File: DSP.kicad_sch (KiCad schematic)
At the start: 24 parts, among them J2 Conn_01x04, J3 MEM2067-02-180-00-A_REVB, J5 Conn_01x04, U4 STM32F401RBTx, Y1 16MHz

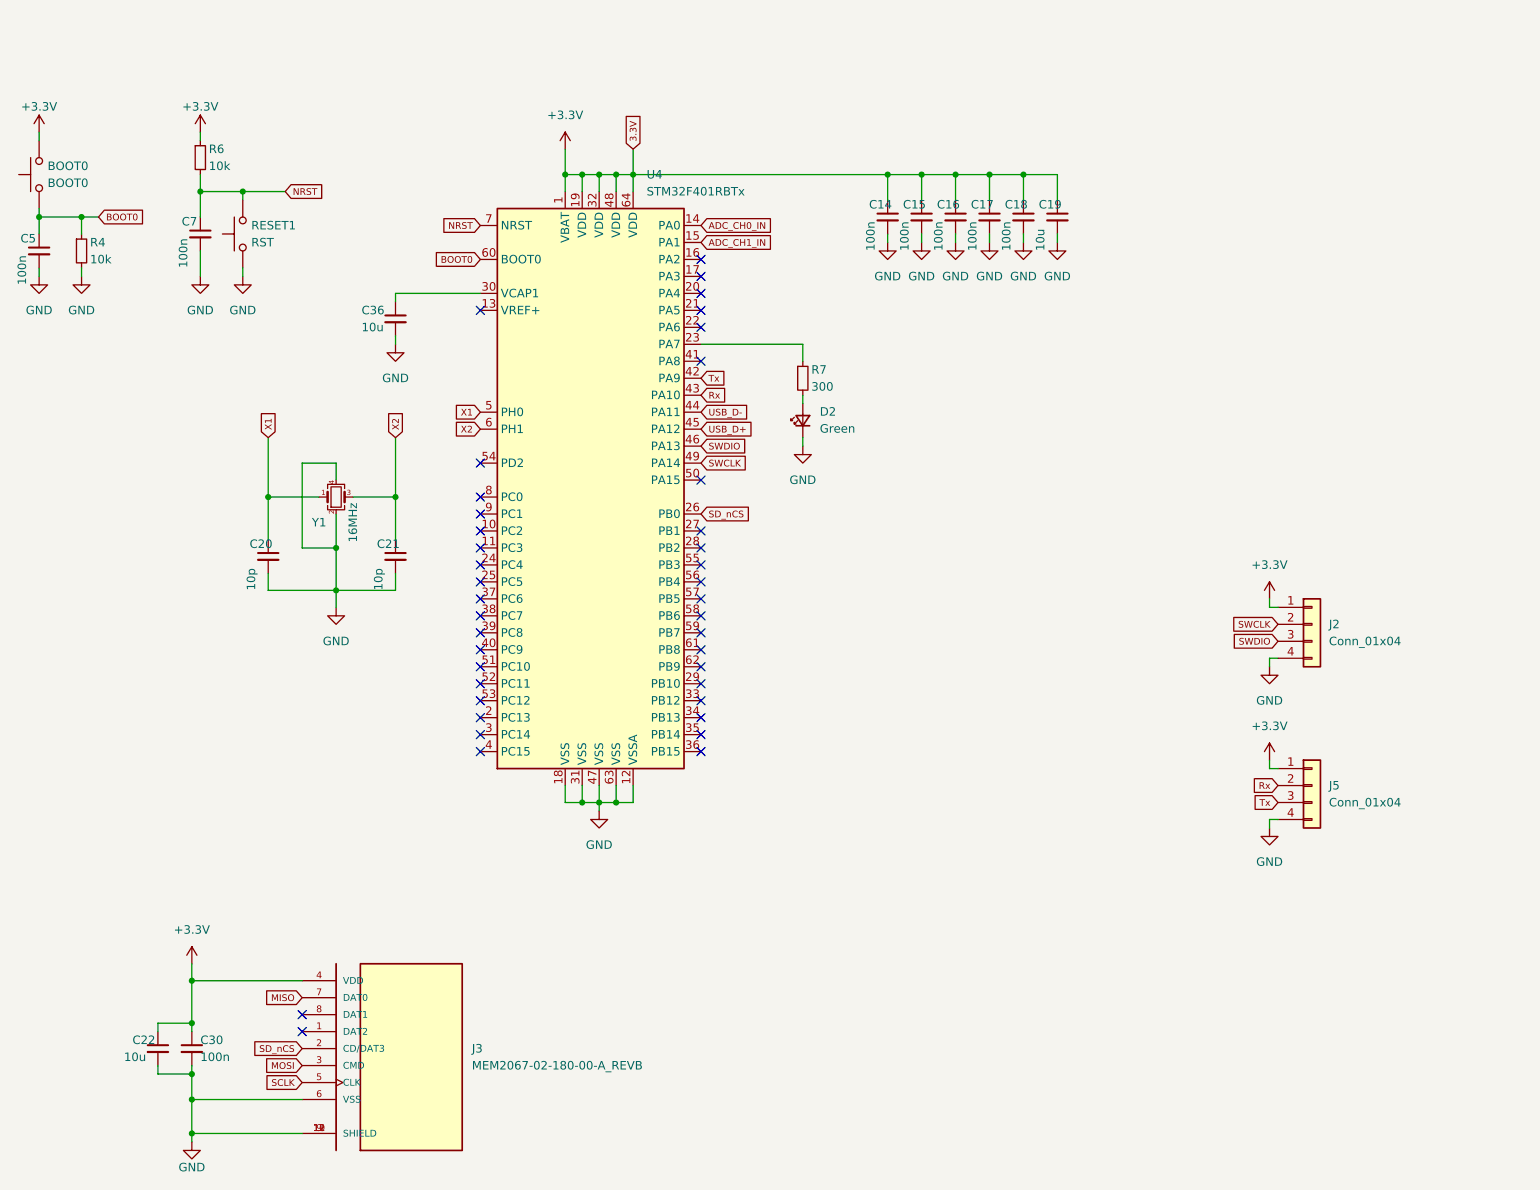
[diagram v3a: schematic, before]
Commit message: made analog circuitry a bit more compact moved whole board
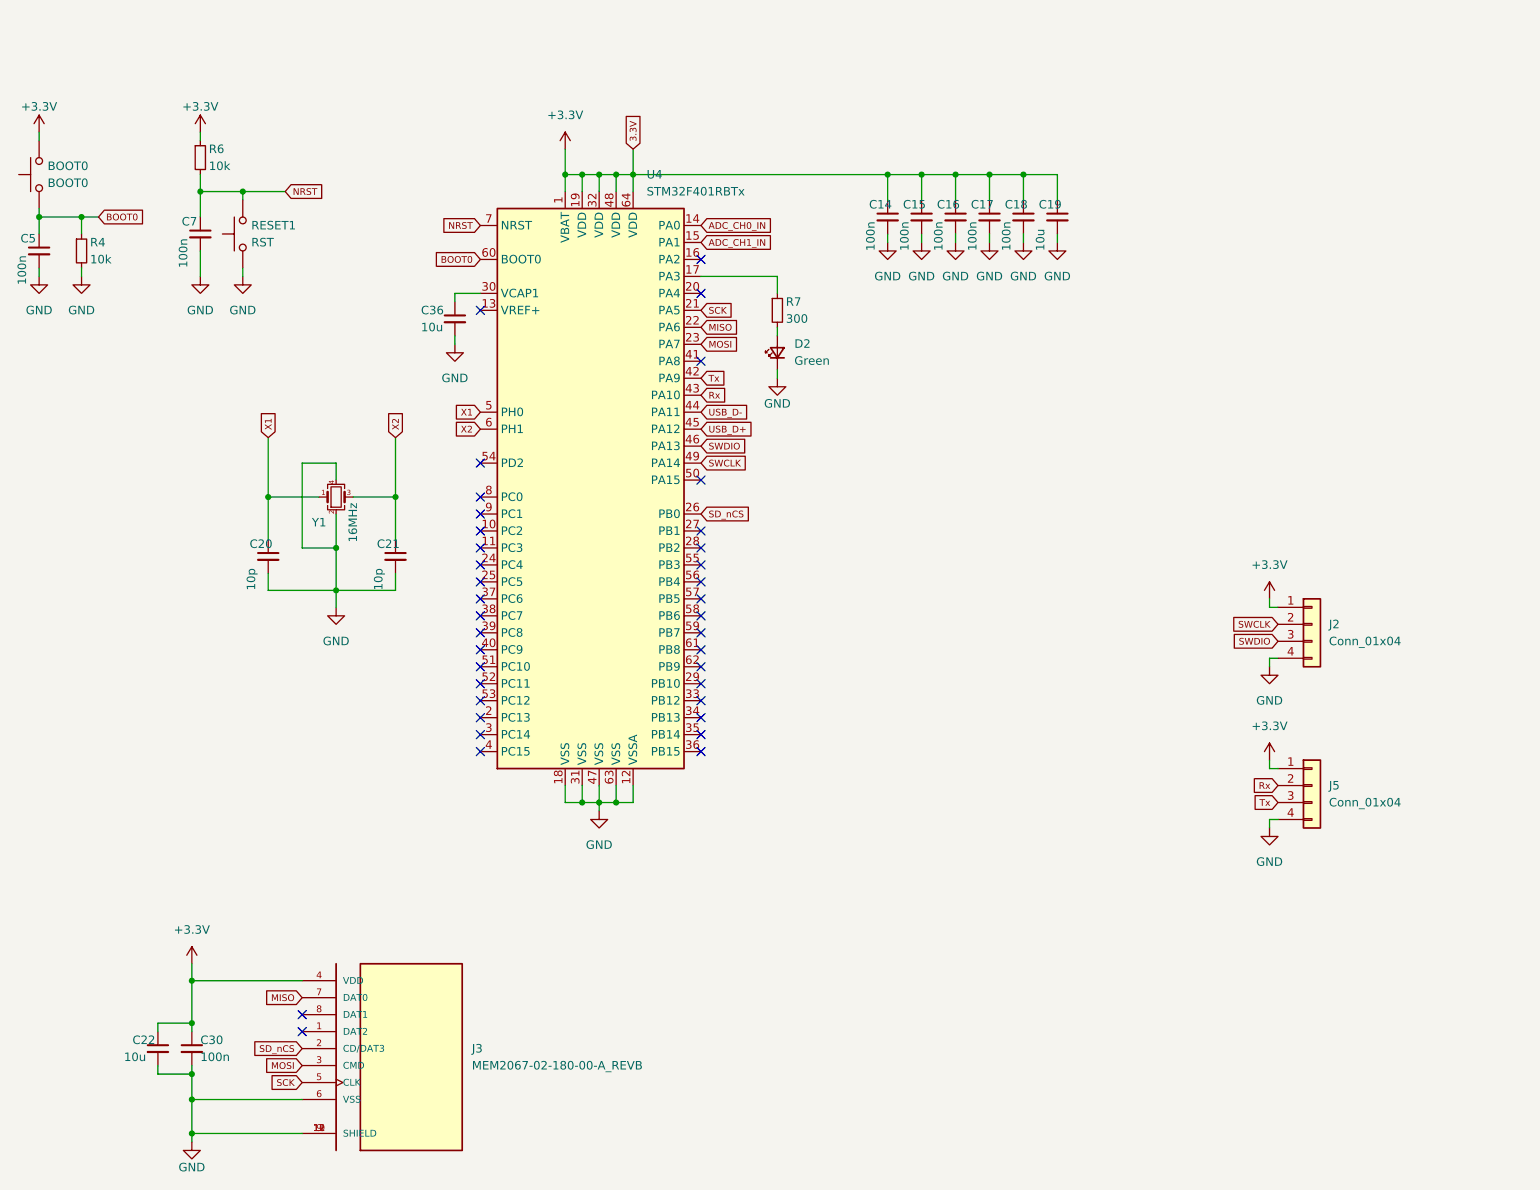
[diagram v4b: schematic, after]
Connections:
- net SCLK is gone; now on net SCK: J3.5 (CLK)
- net MISO: now also U4.22 (PA6)
- net MOSI: now also U4.23 (PA7)
- net at R7.1: now also U4.17 (PA3); no longer U4.23 (PA7)
- net SCK: now reaches U4.21 (PA5)
- no-connect marks 41 -> 38
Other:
- moved on the sheet: C36, D2, R7
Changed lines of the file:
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@@
   (no_connect (at 96.52 77.47))
   (no_connect (at 96.52 87.63))
-  (no_connect (at 129.54 57.15))
   (no_connect (at 129.54 102.87))
   (no_connect (at 96.52 90.17))
-  (no_connect (at 129.54 49.53))
   (no_connect (at 96.52 120.65))
   (no_connect (at 129.54 100.33))
   (no_connect (at 96.52 110.49))
-  (no_connect (at 129.54 54.61))
   (no_connect (at 69.85 162.56))
-  (no_connect (at 129.54 62.23))
   (no_connect (at 96.52 54.61))
   (no_connect (at 129.54 107.95))
@@
   (no_connect (at 129.54 46.99))
   (no_connect (at 96.52 85.09))
+  (no_connect (at 129.54 62.23))
   (no_connect (at 96.52 107.95))
   (no_connect (at 129.54 120.65))
@@
     (stroke (width 0) (type default))
   )
-  (wire (pts (xy 83.82 58.42) (xy 83.82 59.69))
+  (wire (pts (xy 92.71 58.42) (xy 92.71 59.69))
     (stroke (width 0) (type default))
   )
@@
     (stroke (width 0) (type default))
   )
-  (wire (pts (xy 144.78 59.69) (xy 129.54 59.69))
-    (stroke (width 0) (type default))
-  )
   (wire (pts (xy 74.93 80.01) (xy 74.93 77.47))
     (stroke (width 0) (type default))
@@
     (stroke (width 0) (type default))
   )
-  (wire (pts (xy 83.82 52.07) (xy 96.52 52.07))
+  (wire (pts (xy 92.71 52.07) (xy 96.52 52.07))
     (stroke (width 0) (type default))
   )
@@
     (stroke (width 0) (type default))
   )
-  (wire (pts (xy 83.82 53.34) (xy 83.82 52.07))
+  (wire (pts (xy 92.71 53.34) (xy 92.71 52.07))
     (stroke (width 0) (type default))
   )
@@
     (stroke (width 0) (type default))
   )
-  (wire (pts (xy 144.78 73.66) (xy 144.78 74.93))
+  (wire (pts (xy 140.97 63.5) (xy 140.97 64.77))
     (stroke (width 0) (type default))
   )
@@
     (stroke (width 0) (type default))
   )
-  (wire (pts (xy 144.78 62.23) (xy 144.78 59.69))
+  (wire (pts (xy 140.97 52.07) (xy 140.97 49.53))
     (stroke (width 0) (type default))
   )
@@
     (stroke (width 0) (type default))
   )
-  (wire (pts (xy 144.78 67.31) (xy 144.78 68.58))
+  (wire (pts (xy 140.97 57.15) (xy 140.97 58.42))
+    (stroke (width 0) (type default))
+  )
+  (wire (pts (xy 129.54 49.53) (xy 140.97 49.53))
     (stroke (width 0) (type default))
   )
@@
     )
   )
+  (global_label "SCK" (shape input) (at 129.54 54.61 0) (fields_autoplaced)
+    (effects (font (size 1 1)) (justify left))
+    (property "Intersheetrefs" "${INTERSHEET_REFS}" (at 134.7803 54.61 0)
+      (effects (font (size 1 1)) (justify left) hide)
+    )
+  )
   (global_label "Tx" (shape input) (at 215.9 128.27 180) (fields_autoplaced)
     (effects (font (size 1 1)) (justify right))
@@
     )
   )
+  (global_label "MISO" (shape input) (at 129.54 57.15 0) (fields_autoplaced)
+    (effects (font (size 1 1)) (justify left))
+    (property "Intersheetrefs" "${INTERSHEET_REFS}" (at 135.447 57.15 0)
+      (effects (font (size 1 1)) (justify left) hide)
+    )
+  )
   (global_label "SWDIO" (shape input) (at 215.9 104.14 180) (fields_autoplaced)
     (effects (font (size 1 1)) (justify right))
@@
     )
   )
-  (global_label "SCLK" (shape input) (at 69.85 170.18 180) (fields_autoplaced)
+  (global_label "SCK" (shape input) (at 69.85 170.18 180) (fields_autoplaced)
     (effects (font (size 1 1)) (justify right))
-    (property "Intersheetrefs" "${INTERSHEET_REFS}" (at 64.1881 170.1175 0)
+    (property "Intersheetrefs" "${INTERSHEET_REFS}" (at 64.6097 170.18 0)
       (effects (font (size 1 1)) (justify right) hide)
     )
@@
     )
   )
+  (global_label "MOSI" (shape input) (at 129.54 59.69 0) (fields_autoplaced)
+    (effects (font (size 1 1)) (justify left))
+    (property "Intersheetrefs" "${INTERSHEET_REFS}" (at 135.447 59.69 0)
+      (effects (font (size 1 1)) (justify left) hide)
+    )
+  )
   (global_label "ADC_CH1_IN" (shape input) (at 129.54 44.45 0) (fields_autoplaced)
     (effects (font (size 1 1)) (justify left))
@@
     )
   )
-  (symbol (lib_id "Device:LED_Small") (at 144.78 71.12 90) (unit 1)
-    (in_bom yes) (on_board yes) (dnp no) (fields_autoplaced)
-    (property "Reference" "D2" (at 147.32 69.7864 90)
+  (symbol (lib_id "Device:LED_Small") (at 140.97 60.96 90) (unit 1)
+    (in_bom yes) (on_board yes) (dnp no) (fields_autoplaced)
+    (property "Reference" "D2" (at 143.51 59.6264 90)
       (effects (font (size 1.27 1.27)) (justify right))
     )
-    (property "Value" "Green" (at 147.32 72.3264 90)
+    (property "Value" "Green" (at 143.51 62.1664 90)
       (effects (font (size 1.27 1.27)) (justify right))
     )
-    (property "Footprint" "LED_SMD:LED_0603_1608Metric_Pad1.05x0.95mm_HandSolder" (at 144.78 71.12 90)
-      (effects (font (size 1.27 1.27)) hide)
-    )
-    (property "Datasheet" "~" (at 144.78 71.12 90)
+    (property "Footprint" "LED_SMD:LED_0603_1608Metric_Pad1.05x0.95mm_HandSolder" (at 140.97 60.96 90)
+      (effects (font (size 1.27 1.27)) hide)
+    )
+    (property "Datasheet" "~" (at 140.97 60.96 90)
       (effects (font (size 1.27 1.27)) hide)
     )
@@
     )
   )
-  (symbol (lib_id "Device:C_Small") (at 83.82 55.88 0) (unit 1)
-    (in_bom yes) (on_board yes) (dnp no)
-    (property "Reference" "C36" (at 78.74 54.61 0)
-      (effects (font (size 1.27 1.27)) (justify left))
-    )
-    (property "Value" "10u" (at 78.74 57.15 0)
-      (effects (font (size 1.27 1.27)) (justify left))
-    )
-    (property "Footprint" "Capacitor_SMD:C_0603_1608Metric_Pad1.08x0.95mm_HandSolder" (at 83.82 55.88 0)
-      (effects (font (size 1.27 1.27)) hide)
-    )
-    (property "Datasheet" "~" (at 83.82 55.88 0)
+  (symbol (lib_id "Device:C_Small") (at 92.71 55.88 0) (unit 1)
+    (in_bom yes) (on_board yes) (dnp no)
+    (property "Reference" "C36" (at 87.63 54.61 0)
+      (effects (font (size 1.27 1.27)) (justify left))
+    )
+    (property "Value" "10u" (at 87.63 57.15 0)
+      (effects (font (size 1.27 1.27)) (justify left))
+    )
+    (property "Footprint" "Capacitor_SMD:C_0603_1608Metric_Pad1.08x0.95mm_HandSolder" (at 92.71 55.88 0)
+      (effects (font (size 1.27 1.27)) hide)
+    )
+    (property "Datasheet" "~" (at 92.71 55.88 0)
       (effects (font (size 1.27 1.27)) hide)
     )
@@
     )
   )
-  (symbol (lib_id "Device:R_Small") (at 144.78 64.77 0) (unit 1)
-    (in_bom yes) (on_board yes) (dnp no)
-    (property "Reference" "R7" (at 146.05 63.5 0)
-      (effects (font (size 1.27 1.27)) (justify left))
-    )
-    (property "Value" "300" (at 146.05 66.04 0)
-      (effects (font (size 1.27 1.27)) (justify left))
-    )
-    (property "Footprint" "Resistor_SMD:R_0603_1608Metric_Pad0.98x0.95mm_HandSolder" (at 144.78 64.77 0)
-      (effects (font (size 1.27 1.27)) hide)
-    )
-    (property "Datasheet" "~" (at 144.78 64.77 0)
+  (symbol (lib_id "Device:R_Small") (at 140.97 54.61 0) (unit 1)
+    (in_bom yes) (on_board yes) (dnp no)
+    (property "Reference" "R7" (at 142.24 53.34 0)
+      (effects (font (size 1.27 1.27)) (justify left))
+    )
+    (property "Value" "300" (at 142.24 55.88 0)
+      (effects (font (size 1.27 1.27)) (justify left))
+    )
+    (property "Footprint" "Resistor_SMD:R_0603_1608Metric_Pad0.98x0.95mm_HandSolder" (at 140.97 54.61 0)
+      (effects (font (size 1.27 1.27)) hide)
+    )
+    (property "Datasheet" "~" (at 140.97 54.61 0)
       (effects (font (size 1.27 1.27)) hide)
     )
@@
     )
   )
-  (symbol (lib_id "power:GND") (at 83.82 59.69 0) (unit 1)
-    (in_bom yes) (on_board yes) (dnp no) (fields_autoplaced)
-    (property "Reference" "#PWR0172" (at 83.82 66.04 0)
-      (effects (font (size 1.27 1.27)) hide)
-    )
-    (property "Value" "GND" (at 83.82 64.77 0)
-      (effects (font (size 1.27 1.27)))
-    )
-    (property "Footprint" "" (at 83.82 59.69 0)
-      (effects (font (size 1.27 1.27)) hide)
-    )
-    (property "Datasheet" "" (at 83.82 59.69 0)
+  (symbol (lib_id "power:GND") (at 92.71 59.69 0) (unit 1)
+    (in_bom yes) (on_board yes) (dnp no) (fields_autoplaced)
+    (property "Reference" "#PWR0172" (at 92.71 66.04 0)
+      (effects (font (size 1.27 1.27)) hide)
+    )
+    (property "Value" "GND" (at 92.71 64.77 0)
+      (effects (font (size 1.27 1.27)))
+    )
+    (property "Footprint" "" (at 92.71 59.69 0)
+      (effects (font (size 1.27 1.27)) hide)
+    )
+    (property "Datasheet" "" (at 92.71 59.69 0)
       (effects (font (size 1.27 1.27)) hide)
     )
@@
     )
   )
-  (symbol (lib_id "power:GND") (at 144.78 74.93 0) (unit 1)
-    (in_bom yes) (on_board yes) (dnp no) (fields_autoplaced)
-    (property "Reference" "#PWR0142" (at 144.78 81.28 0)
-      (effects (font (size 1.27 1.27)) hide)
-    )
-    (property "Value" "GND" (at 144.78 80.01 0)
-      (effects (font (size 1.27 1.27)))
-    )
-    (property "Footprint" "" (at 144.78 74.93 0)
-      (effects (font (size 1.27 1.27)) hide)
-    )
-    (property "Datasheet" "" (at 144.78 74.93 0)
-      (effects (font (size 1.27 1.27)) hide)
-    )
+  (symbol (lib_id "power:GND") (at 140.97 64.77 0) (unit 1)
+    (in_bom yes) (on_board yes) (dnp no)
+    (property "Reference" "#PWR0142" (at 140.97 71.12 0)
+      (effects (font (size 1.27 1.27)) hide)
+    )
+    (property "Value" "GND" (at 140.97 68.58 0)
+      (effects (font (size 1.27 1.27)))
+    )
+    (property "Footprint" "" (at 140.97 64.77 0)
+      (effects (font (size 1.27 1.27)) hide)
+    )
+    (property "Datasheet" "" (at 140.97 64.77 0)
+      (effects (font (size 1.27 1.27)) hide)
+    )
